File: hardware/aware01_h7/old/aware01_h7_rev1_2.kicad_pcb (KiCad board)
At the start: 4 copper layers, 77.5 x 110 mm, 177 parts, among them IC1 TLV320AIC3204IRHBR, J1 Conn_01x06_Pin, J10 CV2_IN, J11 V/OCT_IN, J12 CV1_IN, J2 Conn_01x03_Pin, J3 Conn_02x05_Odd_Even, J4 InL, J5 InR, J6 OutL, J7 OutR, J8 GATE1_IN, J9 GATE2_IN, Q1 MMBT3904, Q2 MMBT3904, SW1 SW_Push, SW2 SW_Push, SW3 SW_Push, U1 STM32H7B0ZBTx, U10 NE5532DRG4, U11 LMV722IDR, U12 LMV722IDR, U2 IS45S16800F-7TLA2, U3 10k, U4 10k, U5 10k, U6 10k, U7 LM1117MP-3.3, U8 LM4040DIM3X-10, U9 NE5532DRG4, Y1 WE-XTAL 24.0MHz 50ppm

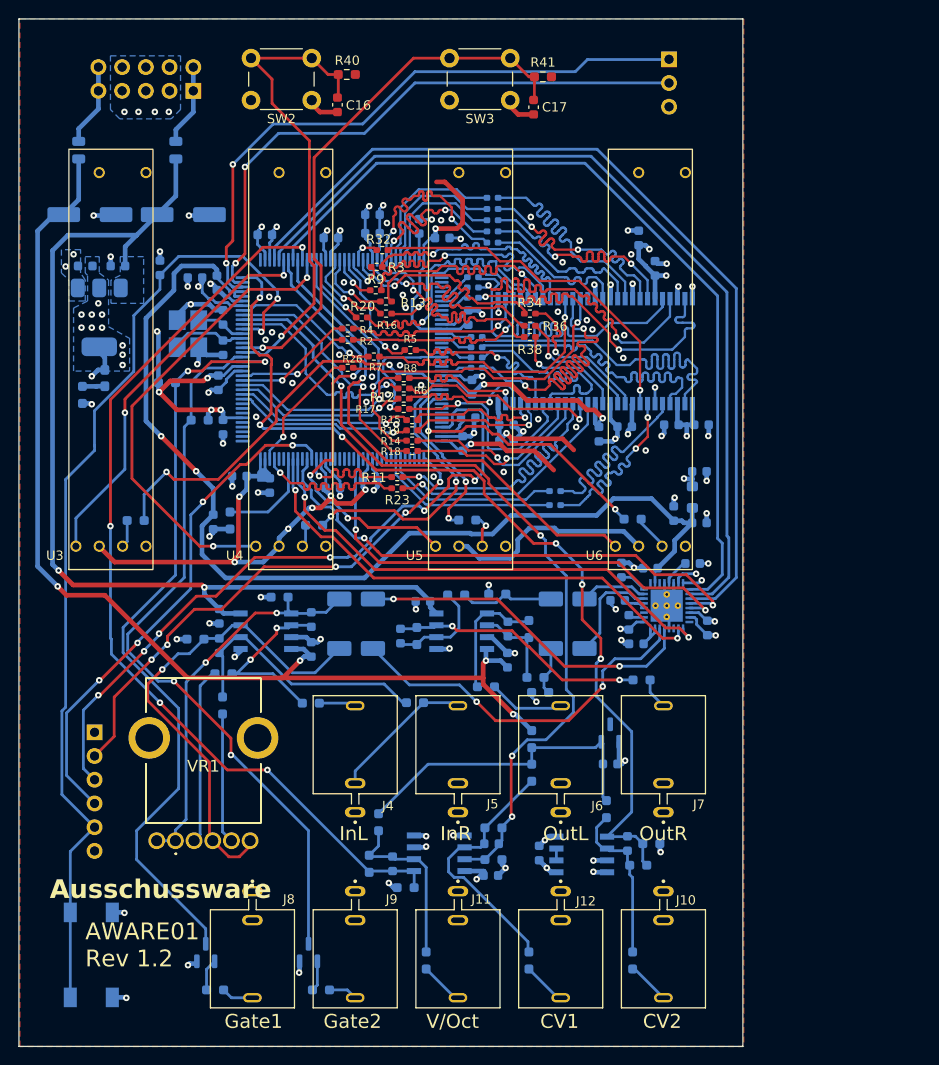
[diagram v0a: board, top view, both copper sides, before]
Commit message: rework layout and insert eletrolytic caps for gainstages
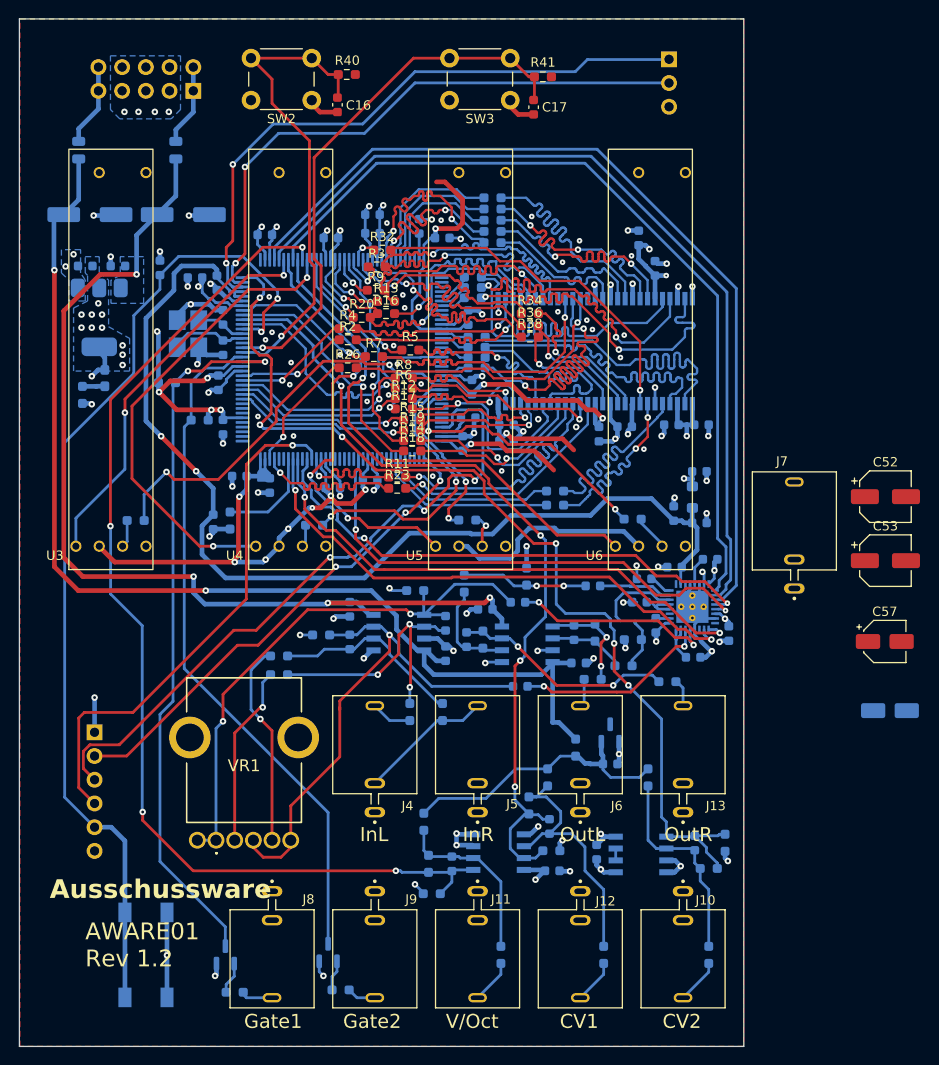
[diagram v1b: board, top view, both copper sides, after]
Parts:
- removed U12: LMV722IDR, Eurorack:LMV722IDR
- added C47: 1u, Capacitor_SMD:C_0603_1608Metric, B.Cu at (168.9, 103.5)
- added C48: 1u, Capacitor_SMD:C_0603_1608Metric, B.Cu at (169.2, 112.5)
- added C52: 10u, Capacitor_SMD:C_0603_1608Metric, B.Cu at (176.9, 101.7)
- added J13: OutR, Eurorack:THONK_PJ398SM-12, F.Cu at (186.6, 119.5)
- added U13: LMV722IDR, Eurorack:LMV722IDR, B.Cu at (166.8, 130.2)
- C52, C53: footprint Capacitor_SMD:CP_Elec_4x5.4 -> Capacitor_SMD:CP_Elec_5x4.5; moved to F.Cu
- C57: moved to F.Cu
- R10, R11, R12, R13, R14, R15, R16, R17, R18, R19, R2, R20, R21, R22, R23, R24, R25, R26, R27, R28, R29, R3, R30, R31, R32, R33, R34, R35, R36, R37, R38, R39, R4, R5, R6, R7, R8, R9: footprint Resistor_SMD:R_0402_1005Metric_Pad0.72x0.64mm_HandSolder -> Resistor_SMD:R_0603_1608Metric_Pad0.98x0.95mm_HandSolder
- moved C52 57.7 mm to (208.3, 92.1)
- moved C53 57.4 mm to (208.3, 99.0)
- moved C56 35.1 mm to (208.8, 115.0), turned to 180 degrees
- moved C57 34.3 mm to (208.2, 107.7)
- moved J7 27.8 mm to (198.5, 95.5)
- moved R52 14.5 mm to (157.9, 102.2)
- moved C49 14.4 mm to (161.2, 109.0)
- moved C50 14.4 mm to (161.2, 105.7)
- moved U9 14.2 mm to (156.2, 106.7)
- moved C48 14.0 mm to (150.9, 104.2)
- moved C51 14.0 mm to (150.9, 107.7)
- moved R53 13.5 mm to (147.8, 107.0)
- moved R60 11.5 mm to (176.9, 111.7), turned to 180 degrees
- moved R54 11.4 mm to (181.2, 107.5)
- moved R48 10.6 mm to (157.3, 115.2), turned to 90 degrees
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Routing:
- net Net-(C45-Pad1): track 0.00 -> 59.8 mm, vias 0 -> 2
- net Net-(C46-Pad1): track 0.00 -> 56.3 mm
- net Net-(C51-Pad1): track 52.9 -> 0.00 mm
- net Net-(C50-Pad1): track 41.5 -> 0.00 mm, vias 2 -> 0
- net Net-(U13B--): track 0.00 -> 28.6 mm
- net Net-(U12B--): track 27.6 -> 0.00 mm
- net Net-(U13A--): track 0.00 -> 18.9 mm
- net /Audio Codec/Input Output Channels/INR: track 39.7 -> 20.9 mm
- net Net-(U12A--): track 18.7 -> 0.00 mm
- net GND: track 171.2 -> 188.3 mm
- net /V_OCT_IN: track 99.9 -> 116.3 mm
- net /Audio Codec/Input Output Channels/INL: track 37.1 -> 21.8 mm
- net Net-(C52-Pad1): track 0.00 -> 13.5 mm, vias 0 -> 2
- net Net-(C57-Pad1): track 10.2 -> 0.00 mm
- net Net-(U9A--): track 19.9 -> 29.2 mm, vias 2 -> 3
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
